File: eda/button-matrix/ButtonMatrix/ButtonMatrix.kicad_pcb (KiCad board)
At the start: 2 copper layers, 87.2 x 87.2 mm, 62 parts, among them J1 Conn_01x12, J2 Conn_01x12

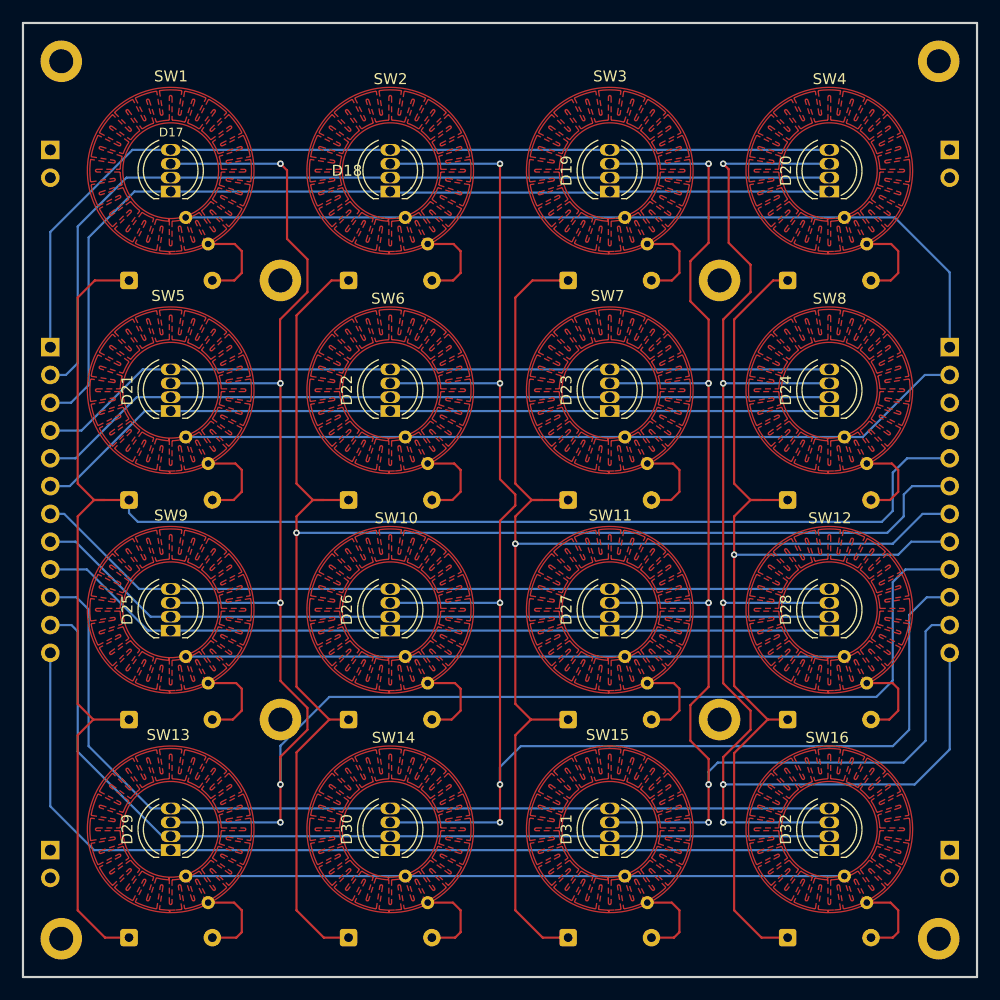
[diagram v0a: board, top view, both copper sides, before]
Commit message: - Fixed silk screen overlap issuess in button pcb
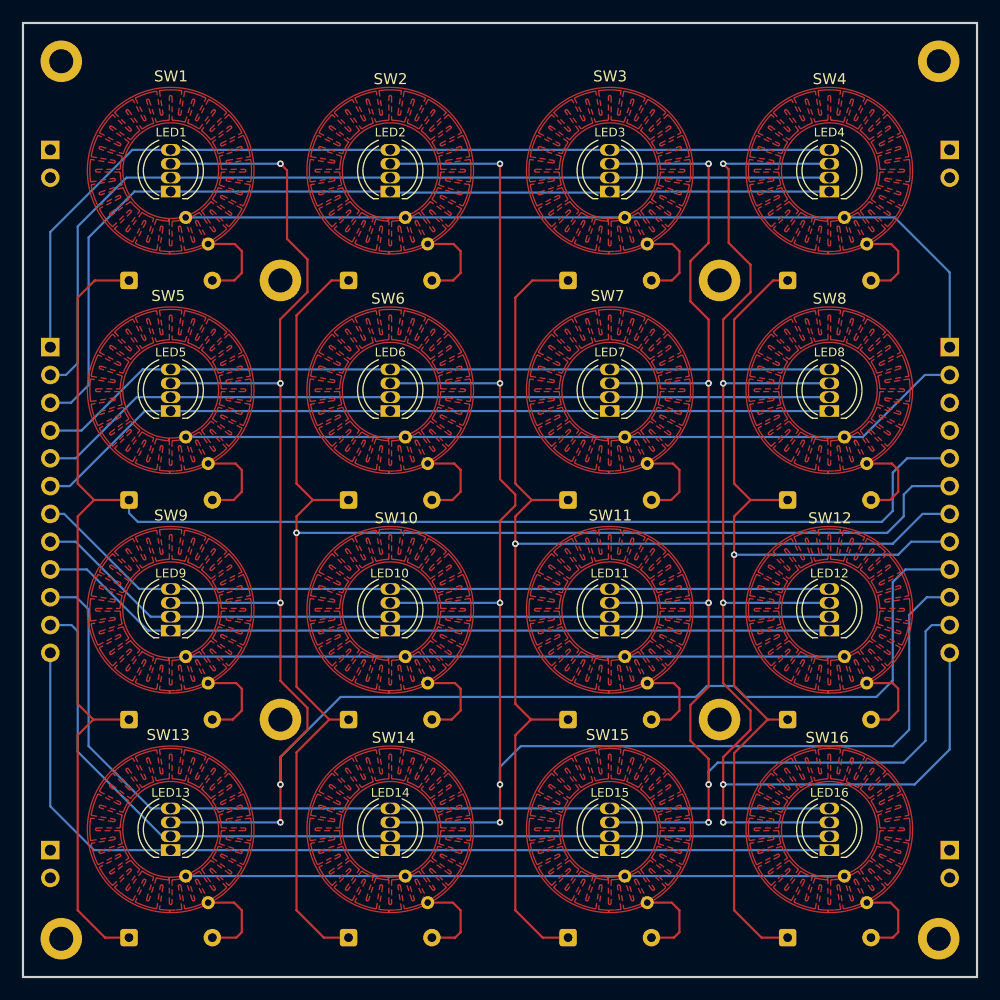
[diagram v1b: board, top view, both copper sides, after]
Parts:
- renumbered D17 to LED1, D26 to LED10, D27 to LED11, D28 to LED12, D29 to LED13, D30 to LED14, D31 to LED15, D32 to LED16, D18 to LED2, D19 to LED3, D20 to LED4, D21 to LED5, D22 to LED6, D23 to LED7, D24 to LED8, D25 to LED9
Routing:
- net /SW_COL4: track 96.5 -> 95.5 mm
- net /SW_COL3: track 118.3 -> 117.3 mm
- net /SW_COL2: track 138.6 -> 137.6 mm
- net /SW_COL1: track 157.9 -> 156.9 mm

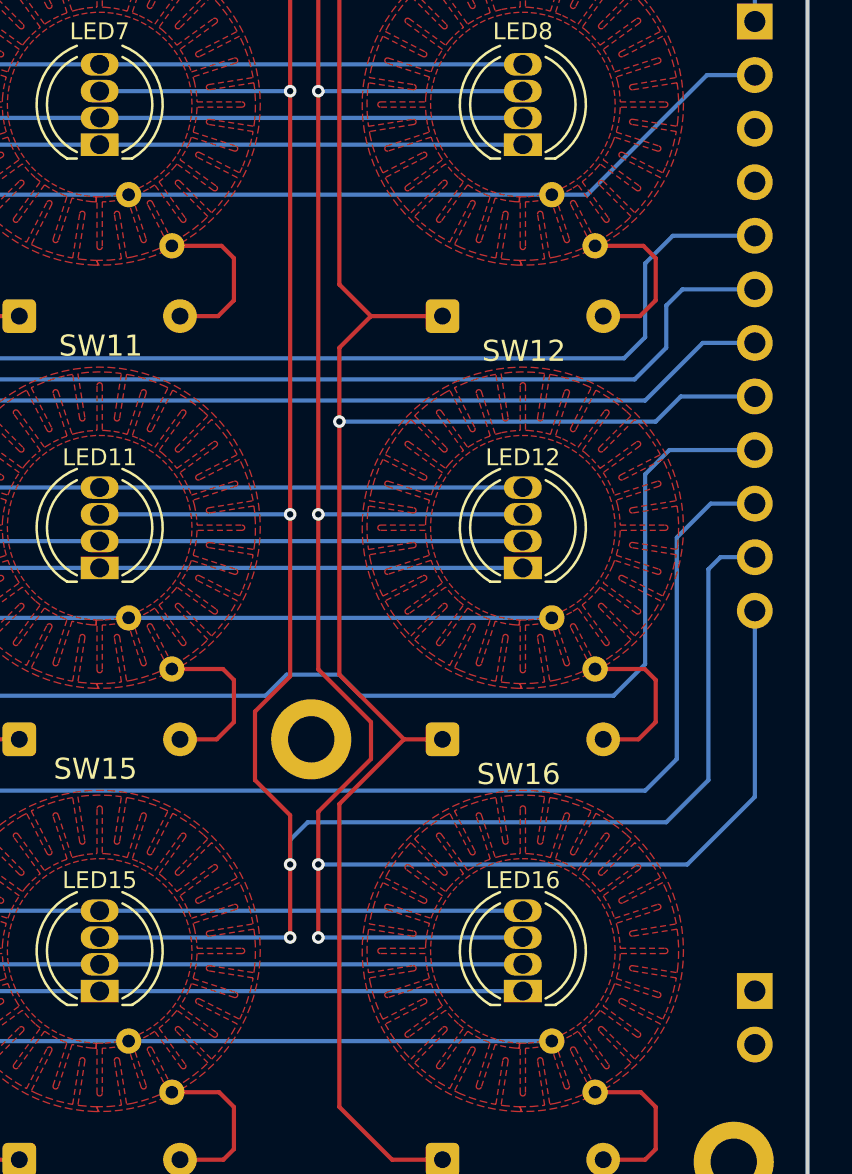
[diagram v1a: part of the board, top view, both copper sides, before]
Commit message: - Completed all connections on pcb and performed design fule check
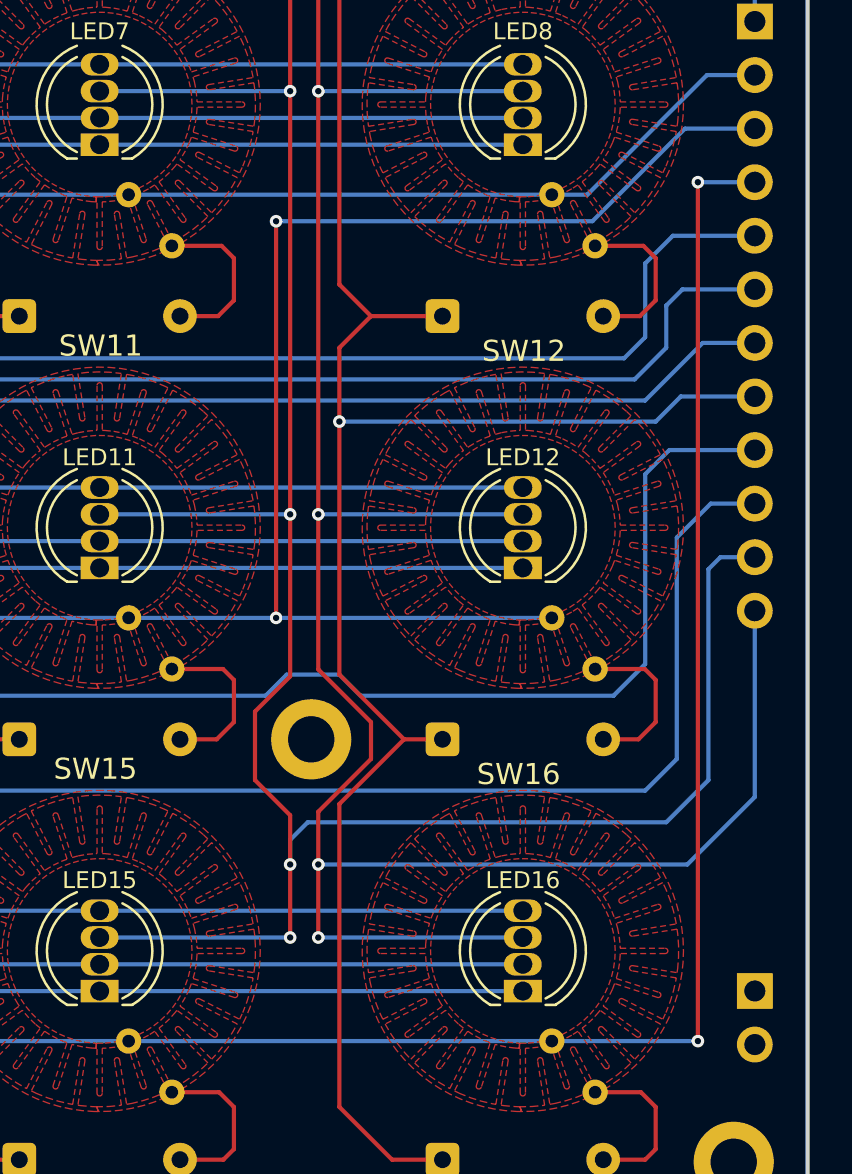
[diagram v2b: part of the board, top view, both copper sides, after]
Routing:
- net /SW_ROW4: track 60.2 -> 110.5 mm, vias 0 -> 2
- net /SW_ROW3: track 60.2 -> 103.5 mm, vias 0 -> 2
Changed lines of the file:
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@@
 			(fill no)
 			(layer "Cmts.User")
-			(net 101446784)
 		)
 		(fp_circle
@@
 			(fill no)
 			(layer "F.CrtYd")
-			(net 101446784)
 		)
 		(fp_text user "${REFERENCE}"
@@
 			(fill no)
 			(layer "Cmts.User")
-			(net 101446784)
 		)
 		(fp_circle
@@
 			(fill no)
 			(layer "F.CrtYd")
-			(net 101446784)
 		)
 		(fp_text user "${REFERENCE}"
@@
 	)
 	(segment
+		(start 190 98.5)
+		(end 190 117.308332)
+		(width 0.2)
+		(layer "F.Cu")
+		(net 23)
+	)
+	(via
+		(at 190 117.308332)
+		(size 0.6)
+		(drill 0.3)
+		(layers "F.Cu" "B.Cu")
+		(net 23)
+	)
+	(via
+		(at 190 98.5)
+		(size 0.6)
+		(drill 0.3)
+		(layers "F.Cu" "B.Cu")
+		(net 23)
+	)
+	(segment
 		(start 183.008332 117.308332)
 		(end 162.941666 117.308332)
@@
 	)
 	(segment
+		(start 209.39 94.11)
+		(end 205 98.5)
+		(width 0.2)
+		(layer "B.Cu")
+		(net 23)
+	)
+	(segment
+		(start 190 98.5)
+		(end 205 98.5)
+		(width 0.2)
+		(layer "B.Cu")
+		(net 23)
+	)
+	(segment
 		(start 142.875 117.308332)
 		(end 162.941666 117.308332)
@@
 	)
 	(segment
-		(start 183.008332 117.308332)
+		(start 190 117.308332)
 		(end 203.075 117.308332)
 		(width 0.2)
@@
 	)
 	(segment
+		(start 212.7 94.11)
+		(end 209.39 94.11)
+		(width 0.2)
+		(layer "B.Cu")
+		(net 23)
+	)
+	(segment
+		(start 183.008332 117.308332)
+		(end 190 117.308332)
+		(width 0.2)
+		(layer "B.Cu")
+		(net 23)
+	)
+	(segment
+		(start 210 137.375)
+		(end 210 96.65)
+		(width 0.2)
+		(layer "F.Cu")
+		(net 24)
+	)
+	(via
+		(at 210 137.375)
+		(size 0.6)
+		(drill 0.3)
+		(layers "F.Cu" "B.Cu")
+		(net 24)
+	)
+	(via
+		(at 210 96.65)
+		(size 0.6)
+		(drill 0.3)
+		(layers "F.Cu" "B.Cu")
+		(net 24)
+	)
+	(segment
 		(start 203.075 137.375)
 		(end 183.008332 137.375)
@@
 	)
 	(segment
+		(start 210 137.375)
+		(end 203.075 137.375)
+		(width 0.2)
+		(layer "B.Cu")
+		(net 24)
+	)
+	(segment
 		(start 142.875 137.375)
 		(end 162.941666 137.375)
 		(width 0.2)
 		(layer "B.Cu")
+		(net 24)
+	)
+	(segment
+		(start 212.7 96.65)
+		(end 210 96.65)
+		(width 0.2)
+		(layer "B.Cu")

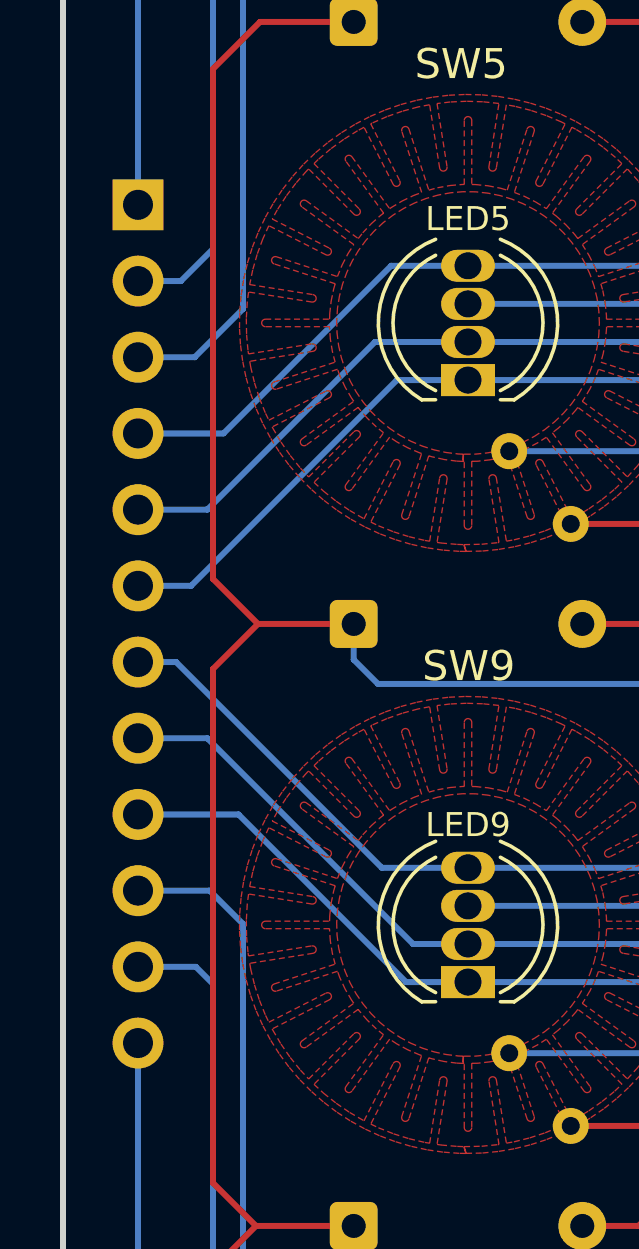
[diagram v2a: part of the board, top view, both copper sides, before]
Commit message: - Added rgb silkscreens to label header pins.
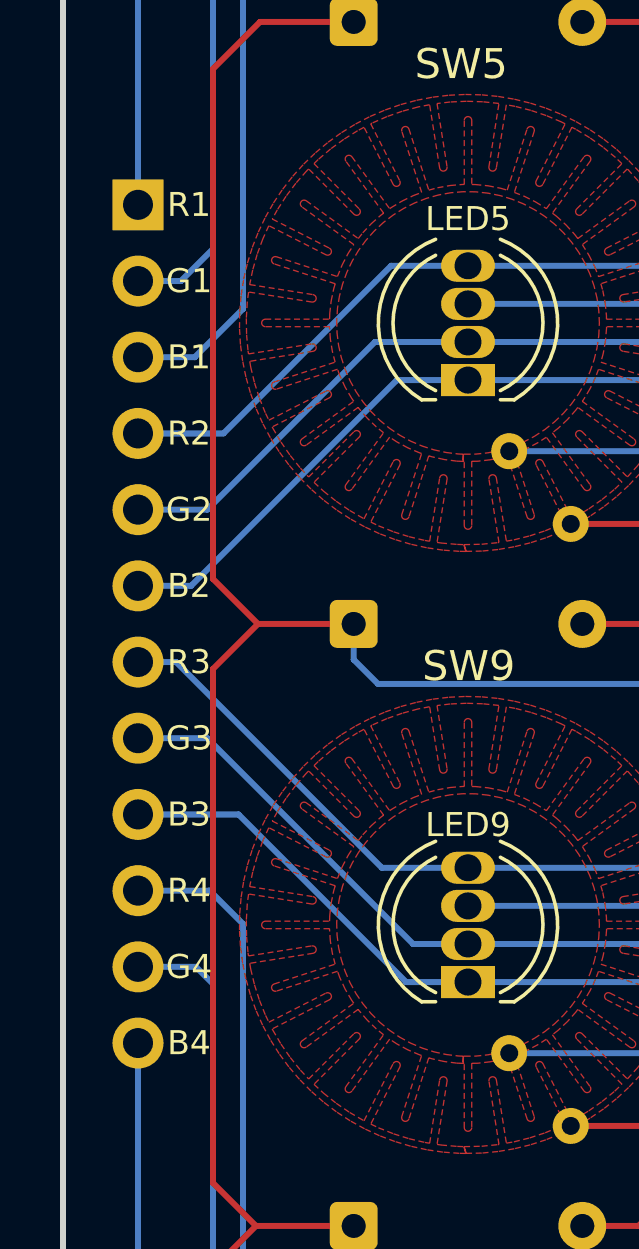
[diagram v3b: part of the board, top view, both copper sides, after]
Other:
- board text added: "B1"
- board text added: "B2"
- board text added: "B3"
- board text added: "B4"
- board text added: "G1"
- board text added: "G2"
- board text added: "G3"
- board text added: "G4"
- board text added: "R1"
- board text added: "R2"
- board text added: "R3"
- board text added: "R4"
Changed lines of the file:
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@@
 		(layer "Edge.Cuts")
+	)
+	(gr_text "R2"
+		(at 132.2 96.65 0)
+		(layer "F.SilkS")
+		(effects
+			(font
+				(size 0.8 0.8)
+				(thickness 0.15)
+			)
+		)
+	)
+	(gr_text "R4"
+		(at 132.2 111.89 0)
+		(layer "F.SilkS")
+		(effects
+			(font
+				(size 0.8 0.8)
+				(thickness 0.15)
+			)
+		)
+	)
+	(gr_text "B1"
+		(at 132.2 94.11 0)
+		(layer "F.SilkS")
+		(effects
+			(font
+				(size 0.8 0.8)
+				(thickness 0.15)
+			)
+		)
+	)
+	(gr_text "B3"
+		(at 132.2 109.35 0)
+		(layer "F.SilkS")
+		(effects
+			(font
+				(size 0.8 0.8)
+				(thickness 0.15)
+			)
+		)
+	)
+	(gr_text "G1"
+		(at 132.2 91.57 0)
+		(layer "F.SilkS")
+		(effects
+			(font
+				(size 0.8 0.8)
+				(thickness 0.15)
+			)
+		)
+	)
+	(gr_text "G4"
+		(at 132.2 114.43 0)
+		(layer "F.SilkS")
+		(effects
+			(font
+				(size 0.8 0.8)
+				(thickness 0.15)
+			)
+		)
+	)
+	(gr_text "R1"
+		(at 132.2 89.03 0)
+		(layer "F.SilkS")
+		(effects
+			(font
+				(size 0.8 0.8)
+				(thickness 0.15)
+			)
+		)
+	)
+	(gr_text "G2"
+		(at 132.2 99.19 0)
+		(layer "F.SilkS")
+		(effects
+			(font
+				(size 0.8 0.8)
+				(thickness 0.15)
+			)
+		)
+	)
+	(gr_text "B2"
+		(at 132.2 101.73 0)
+		(layer "F.SilkS")
+		(effects
+			(font
+				(size 0.8 0.8)
+				(thickness 0.15)
+			)
+		)
+	)
+	(gr_text "B4"
+		(at 132.2 116.97 0)
+		(layer "F.SilkS")
+		(effects
+			(font
+				(size 0.8 0.8)
+				(thickness 0.15)
+			)
+		)
+	)
+	(gr_text "R3"
+		(at 132.2 104.27 0)
+		(layer "F.SilkS")
+		(effects
+			(font
+				(size 0.8 0.8)
+				(thickness 0.15)
+			)
+		)
+	)
+	(gr_text "G3"
+		(at 132.2 106.81 0)
+		(layer "F.SilkS")
+		(effects
+			(font
+				(size 0.8 0.8)
+				(thickness 0.15)
+			)
+		)
 	)
 	(segment
